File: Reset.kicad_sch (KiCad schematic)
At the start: 30 parts, among them U10 74LVC1G04, U4 74LVC1G04, U6 74LVC1G04, U7 74LVC1G04, U8 74LVC1G04, U9 74LVC1G04

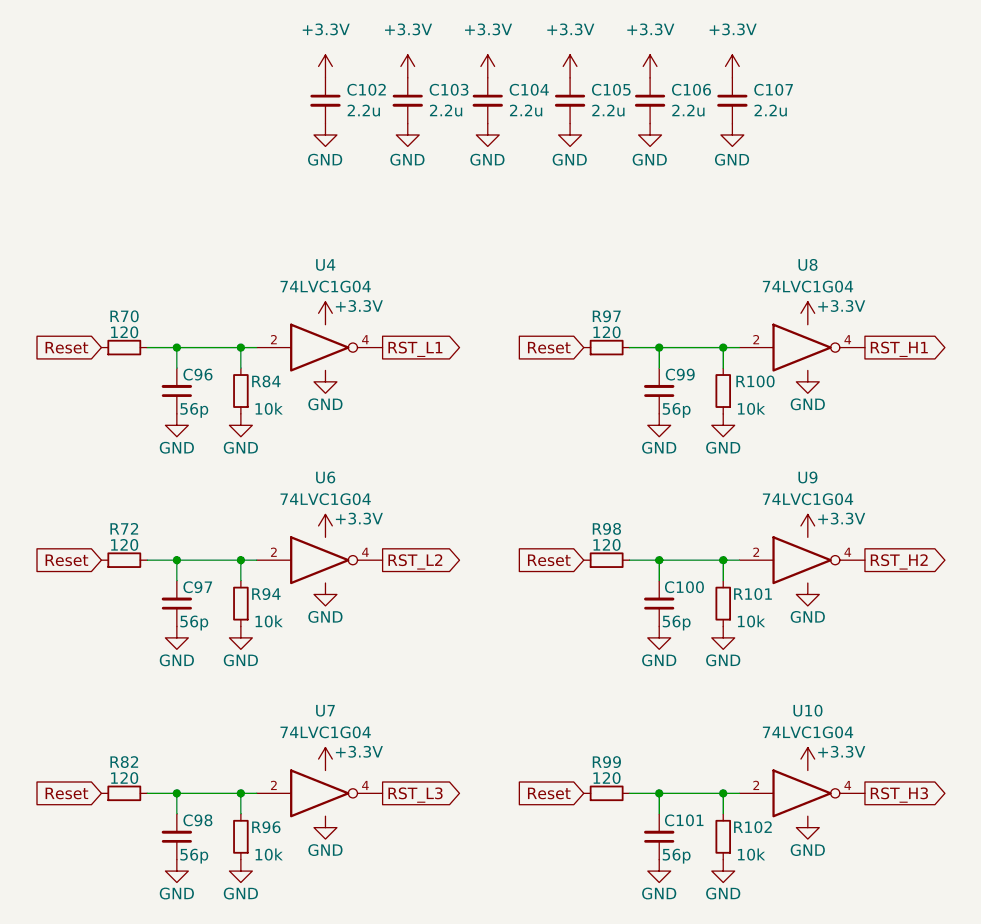
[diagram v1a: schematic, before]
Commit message: Изменил схему
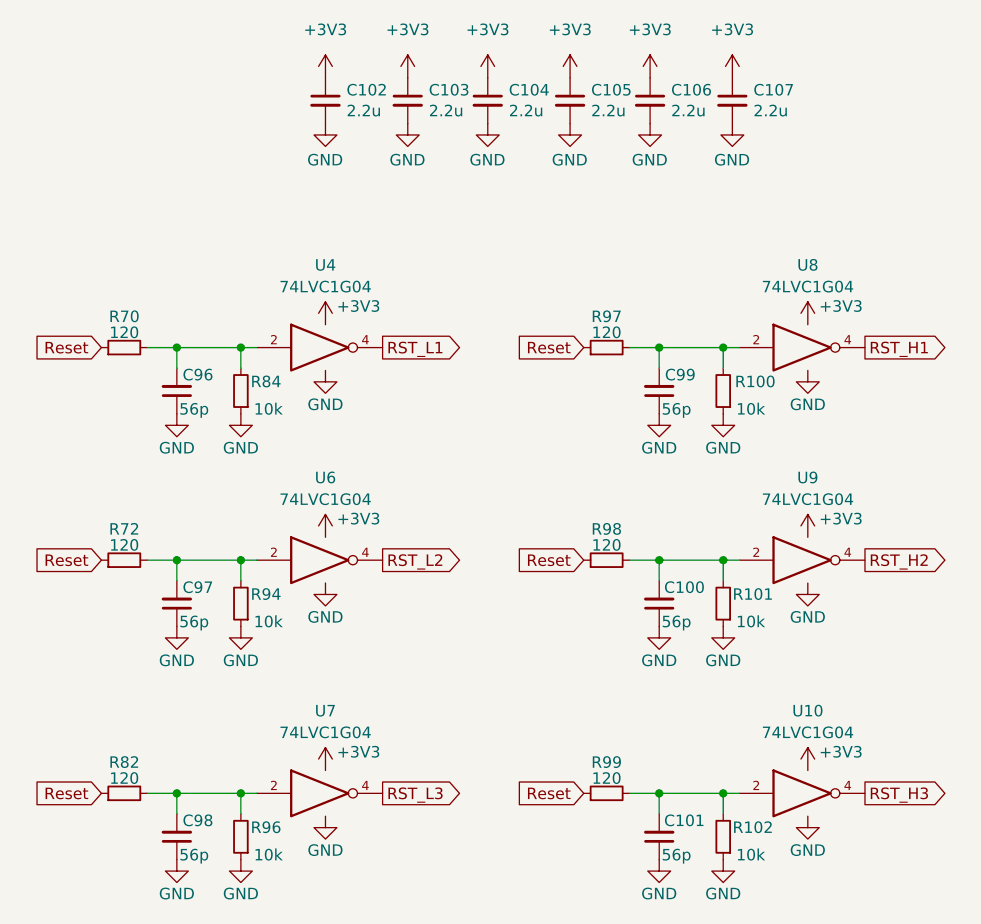
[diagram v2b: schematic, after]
